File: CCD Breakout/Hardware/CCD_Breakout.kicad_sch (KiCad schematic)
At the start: 1 part

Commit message: //WIP CCD Breakout
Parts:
- added J1: Conn_01x03_Pin, symbol Connector:Conn_01x03_Pin
- added Q1: BSS138, Package_TO_SOT_SMD:SOT-23, symbol Transistor_FET:BSS138
- U1: value ~ -> ILX511
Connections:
- net +5V: now also J1.1 (Pin_1)
- net GND: now also J1.3 (Pin_3), Q1.1 (G)
- net SHSW: now also J1.2 (Pin_2)
- removed net NC: U1.10 (NC), U1.13 (NC), U1.14 (NC), U1.7 (NC), U1.8 (NC)
- no-connect marks 0 -> 5

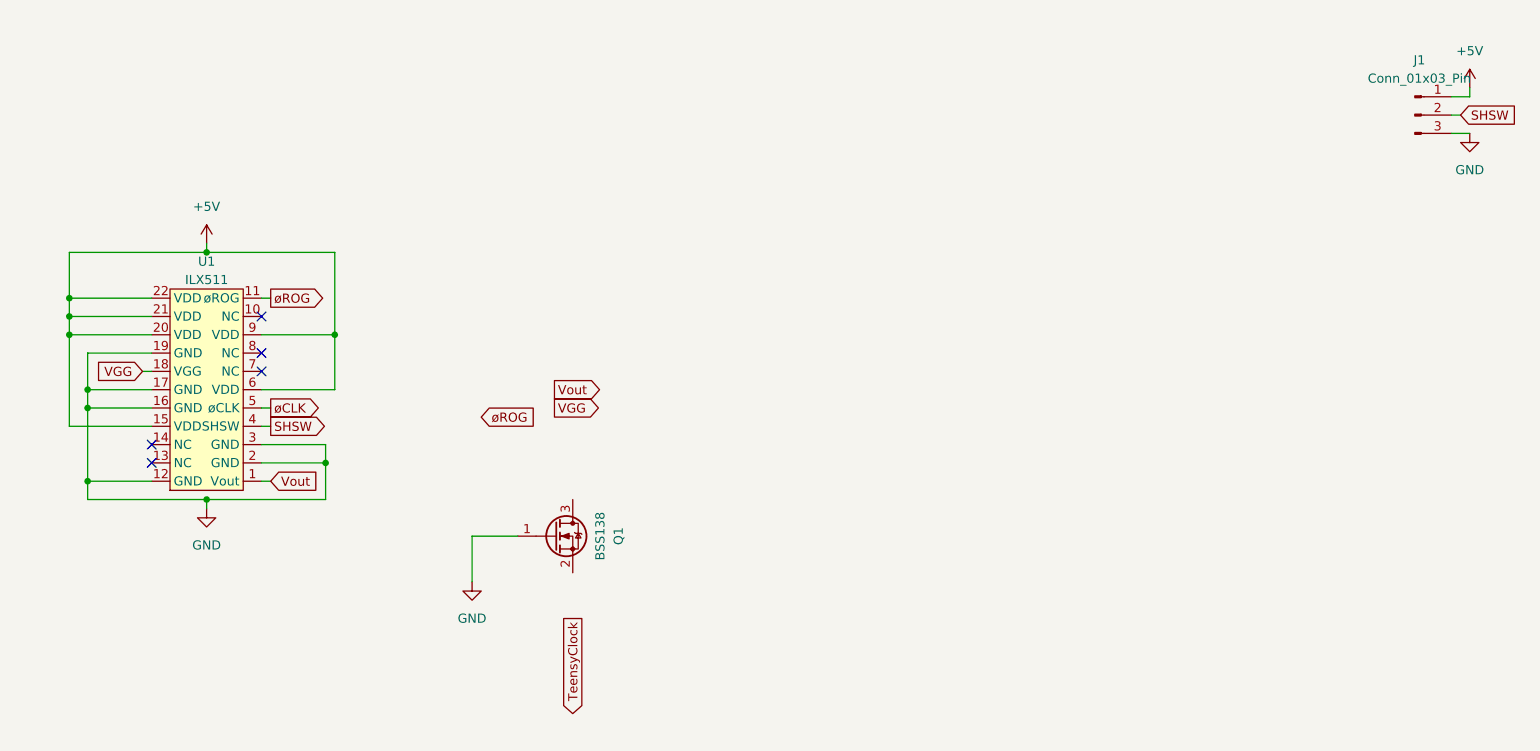
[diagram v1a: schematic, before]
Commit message: Finshed CCD breakout
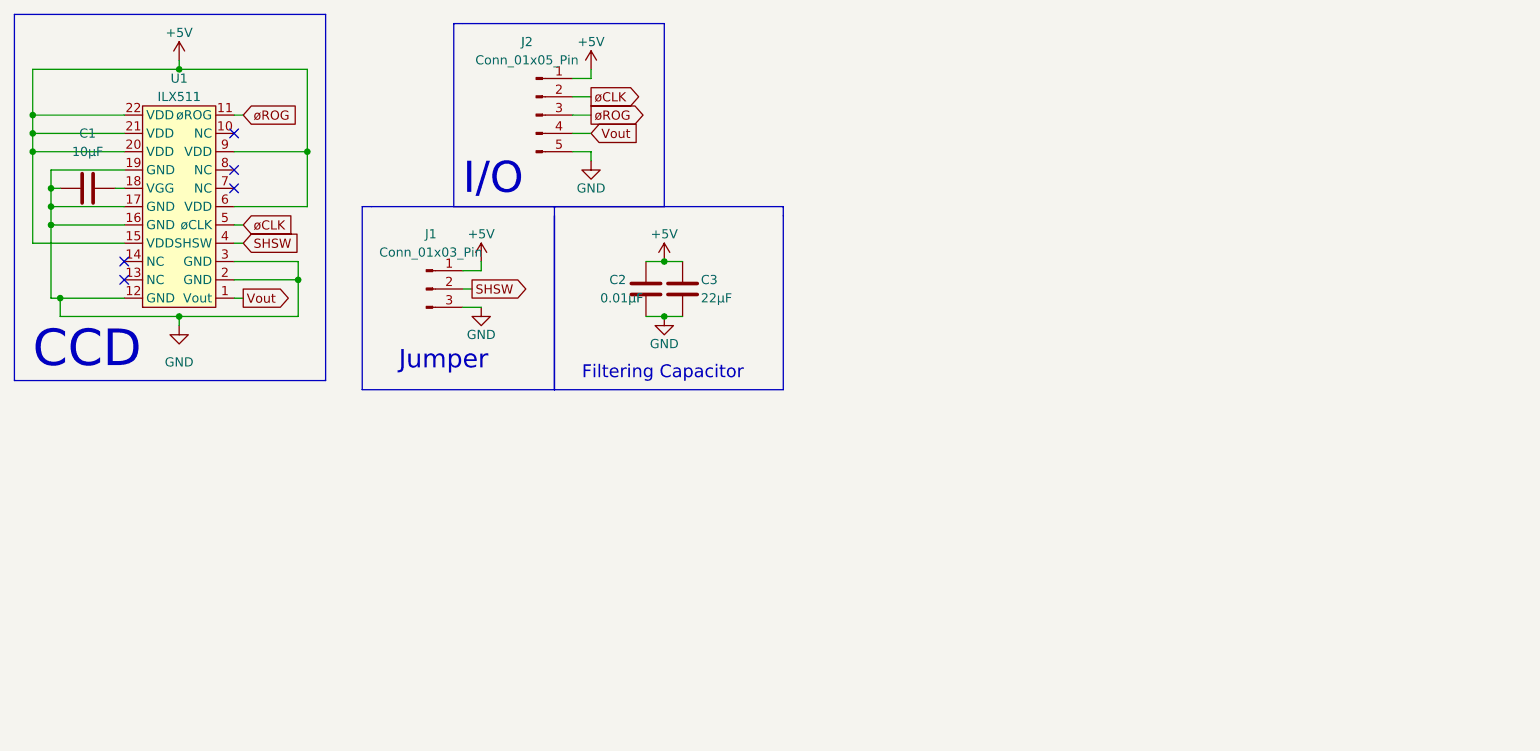
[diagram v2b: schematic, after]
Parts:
- removed Q1: BSS138, Package_TO_SOT_SMD:SOT-23, symbol Transistor_FET:BSS138
- added C1: 10µF, symbol Device:C
- added C2: 0.01µF, symbol Device:C
- added C3: 22µF, symbol Device:C
- added J2: Conn_01x05_Pin, symbol Connector:Conn_01x05_Pin
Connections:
- net +5V: now also C2.2, C3.2, J2.1 (Pin_1)
- net GND: now also C1.1, C2.1, C3.1, J2.5 (Pin_5)
- net Vout: now also J2.4 (Pin_4)
- net øCLK: now also J2.2 (Pin_2)
- net øROG: now also J2.3 (Pin_3)
- net VGG: no longer names the net of U1.18 (VGG)
- net VGG: now also C1.2
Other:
- note added: "CCD"
- note added: "Filtering Capacitor"
- note added: "I/O"
- note added: "Jumper"
- company: (none) ->  
- title: (none) -> Ramen CCD Breakout 
- moved on the sheet: J1, U1

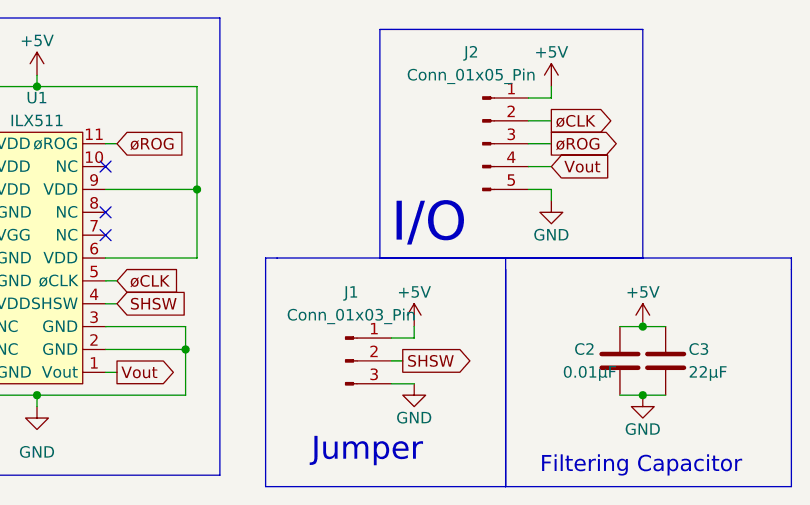
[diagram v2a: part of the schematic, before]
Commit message: fix: switched connectors to Molex
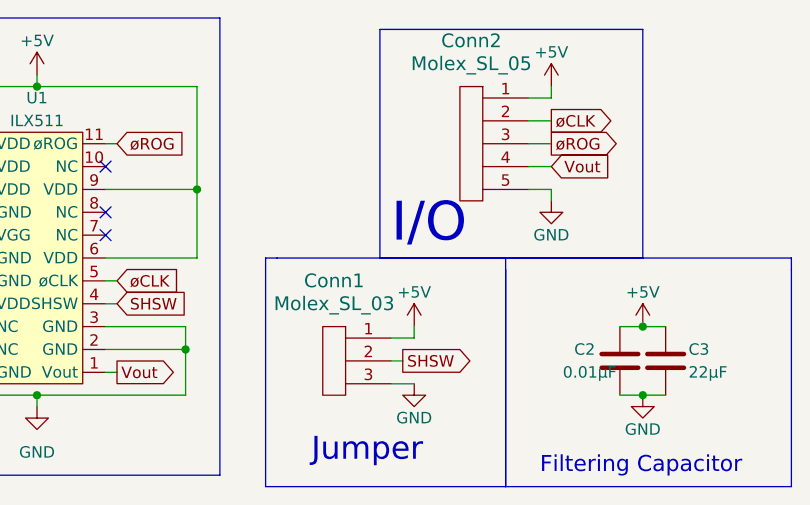
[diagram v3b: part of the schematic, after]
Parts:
- removed J1: Conn_01x03_Pin, symbol Connector:Conn_01x03_Pin
- removed J2: Conn_01x05_Pin, symbol Connector:Conn_01x05_Pin
- added Conn1: Molex_SL_03, symbol MRDT_Connectors:Molex_SL_03
- added Conn2: Molex_SL_05, symbol MRDT_Connectors:Molex_SL_05
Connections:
- net +5V: now also Conn1.1, Conn2.1
- net GND: now also Conn1.3, Conn2.5
- net SHSW: now also Conn1.2
- net Vout: now also Conn2.4
- net øCLK: now also Conn2.2
- net øROG: now also Conn2.3
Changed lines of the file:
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@@
-    )
-  )
-  (symbol (lib_id "Connector:Conn_01x05_Pin") (at 85.09 26.67 0) (unit 1)
-    (in_bom yes) (on_board yes) (dnp no)
-    (property "Reference" "J2" (at 83.82 16.51 0)
-      (effects (font (size 1.27 1.27)))
-    )
-    (property "Value" "Conn_01x05_Pin" (at 83.82 19.05 0)
-      (effects (font (size 1.27 1.27)))
-    )
-    (property "Footprint" "" (at 85.09 26.67 0)
-      (effects (font (size 1.27 1.27)) hide)
-    )
-    (property "Datasheet" "~" (at 85.09 26.67 0)
-      (effects (font (size 1.27 1.27)) hide)
-    )
-    (pin "1")
-    (pin "2")
-    (pin "3")
-    (pin "4")
-    (pin "5")
-    (instances
-      (project "CCD_Breakout"
-        (path "/64b006a0-b432-4c05-bc21-eb3325874dfb"
-          (reference "J2") (unit 1)
-        )
-      )
     )
   )
@@
     )
   )
-  (symbol (lib_id "Connector:Conn_01x03_Pin") (at 69.85 50.8 0) (unit 1)
-    (in_bom yes) (on_board yes) (dnp no)
-    (property "Reference" "J1" (at 70.485 43.18 0)
-      (effects (font (size 1.27 1.27)))
+  (symbol (lib_id "MRDT_Connectors:Molex_SL_03") (at 69.85 54.61 0) (mirror y) (unit 1)
+    (in_bom yes) (on_board yes) (dnp no) (fields_autoplaced)
+    (property "Reference" "Conn1" (at 68.58 41.91 0)
+      (effects (font (size 1.524 1.524)))
     )
-    (property "Value" "Conn_01x03_Pin" (at 70.485 45.72 0)
-      (effects (font (size 1.27 1.27)))
+    (property "Value" "Molex_SL_03" (at 68.58 44.45 0)
+      (effects (font (size 1.524 1.524)))
     )
-    (property "Footprint" "" (at 69.85 50.8 0)
-      (effects (font (size 1.27 1.27)) hide)
+    (property "Footprint" "" (at 69.85 54.61 0)
+      (effects (font (size 1.524 1.524)) hide)
     )
-    (property "Datasheet" "~" (at 69.85 50.8 0)
-      (effects (font (size 1.27 1.27)) hide)
+    (property "Datasheet" "" (at 69.85 54.61 0)
+      (effects (font (size 1.524 1.524)) hide)
     )
     (pin "1")
@@
       (project "CCD_Breakout"
         (path "/64b006a0-b432-4c05-bc21-eb3325874dfb"
-          (reference "J1") (unit 1)
+          (reference "Conn1") (unit 1)
         )
       )
@@
         )
       )
+    )
+  )
+  (symbol (lib_id "MRDT_Connectors:Molex_SL_05") (at 85.09 33.02 0) (mirror y) (unit 1)
+    (in_bom yes) (on_board yes) (dnp no) (fields_autoplaced)
+    (property "Reference" "Conn2" (at 83.82 15.24 0)
+      (effects (font (size 1.524 1.524)))
+    )
+    (property "Value" "Molex_SL_05" (at 83.82 17.78 0)
+      (effects (font (size 1.524 1.524)))
+    )
+    (property "Footprint" "" (at 85.09 33.02 0)
+      (effects (font (size 1.524 1.524)) hide)
+    )
+    (property "Datasheet" "" (at 85.09 33.02 0)
+      (effects (font (size 1.524 1.524)) hide)
+    )
+    (pin "1")
+    (pin "2")
+    (pin "3")
+    (pin "4")
+    (pin "5")
+    (instances
+      (project "CCD_Breakout"
+        (path "/64b006a0-b432-4c05-bc21-eb3325874dfb"
+          (reference "Conn2") (unit 1)
+        )
+      )

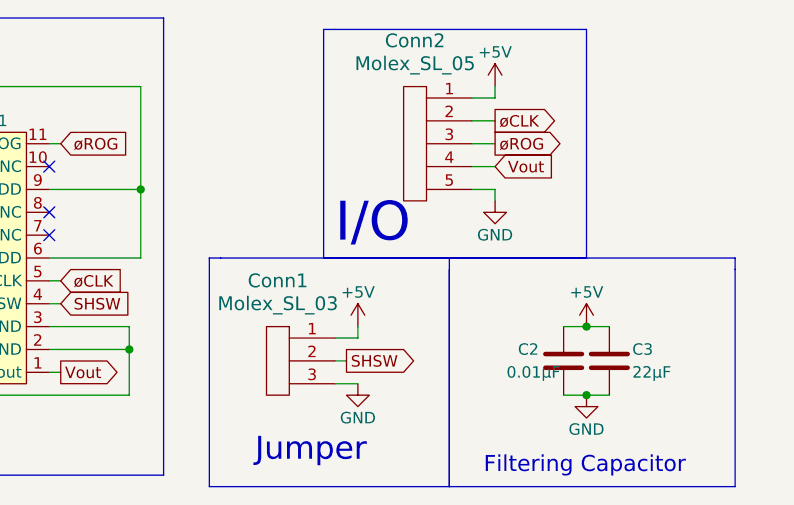
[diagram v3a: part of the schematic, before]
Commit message: fix: replaced net labels with text
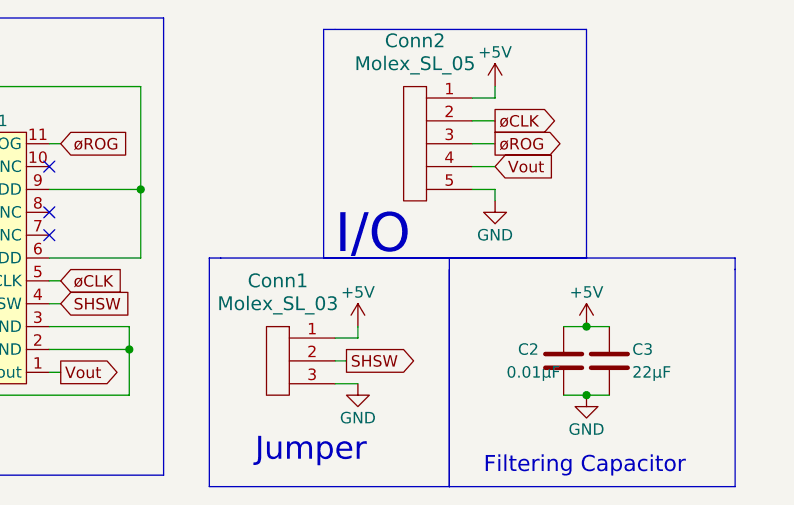
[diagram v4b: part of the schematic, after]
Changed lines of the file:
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@@
     (effects (font (size 1.778 1.778)) (justify left bottom))
   )
-  (text "I/O" (at 74.93 38.1 0)
+  (text "I/O" (at 74.93 39.37 0)
     (effects (font (size 4.318 4.318)) (justify left bottom))
   )

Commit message: misc schematic review changes
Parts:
- removed Conn1: Molex_SL_03, symbol MRDT_Connectors:Molex_SL_03
- added J1: Conn_01x03_Pin, symbol Connector:Conn_01x03_Pin
- renumbered Conn2 to Conn1
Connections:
- net +5V: now also J1.1 (Pin_1)
- net GND: now also J1.3 (Pin_3)
- net SHSW: now also J1.2 (Pin_2)
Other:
- moved on the sheet: C2, C3, Conn1

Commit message: fix: use mosfets to control diodes
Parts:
- Conn1: footprint (none) -> MRDT_Connectors:MOLEX_SL_05_Vertical
- J1: footprint (none) -> Connector_PinHeader_2.54mm:PinHeader_1x03_P2.54mm_Vertical
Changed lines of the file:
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@@
       (effects (font (size 1.27 1.27)))
     )
-    (property "Footprint" "" (at 69.85 48.26 0)
+    (property "Footprint" "Connector_PinHeader_2.54mm:PinHeader_1x03_P2.54mm_Vertical" (at 69.85 48.26 0)
       (effects (font (size 1.27 1.27)) hide)
     )
@@
       (effects (font (size 1.524 1.524)))
     )
-    (property "Footprint" "" (at 100.33 55.88 0)
+    (property "Footprint" "MRDT_Connectors:MOLEX_SL_05_Vertical" (at 100.33 55.88 0)
       (effects (font (size 1.524 1.524)) hide)
     )

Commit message: added footprints to ccd breakout
added all capacitors
the only footprint left is the ccd
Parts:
- C1, C2: footprint (none) -> Capacitor_SMD:C_0603_1608Metric_Pad1.08x0.95mm_HandSolder
- C3: footprint (none) -> Capacitor_SMD:C_0201_0603Metric_Pad0.64x0.40mm_HandSolder
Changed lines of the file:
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@@
       (effects (font (size 1.27 1.27)))
     )
-    (property "Footprint" "" (at 26.67 35.8648 0)
+    (property "Footprint" "Capacitor_SMD:C_0603_1608Metric_Pad1.08x0.95mm_HandSolder" (at 26.67 35.8648 0)
       (effects (font (size 1.27 1.27)) hide)
     )
@@
       (effects (font (size 1.27 1.27)) (justify right))
     )
-    (property "Footprint" "" (at 70.1548 24.13 0)
+    (property "Footprint" "Capacitor_SMD:C_0603_1608Metric_Pad1.08x0.95mm_HandSolder" (at 70.1548 24.13 0)
       (effects (font (size 1.27 1.27)) hide)
     )
@@
       (effects (font (size 1.27 1.27)) (justify right))
     )
-    (property "Footprint" "" (at 75.2348 24.13 0)
+    (property "Footprint" "Capacitor_SMD:C_0201_0603Metric_Pad0.64x0.40mm_HandSolder" (at 75.2348 24.13 0)
       (effects (font (size 1.27 1.27)) hide)
     )

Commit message: created ilx511 footprint
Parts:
- U1: footprint (none) -> MRDT_CCD:ILX511
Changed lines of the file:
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@@
       (effects (font (size 1.27 1.27)))
     )
-    (property "Footprint" "" (at 43.18 40.64 0)
+    (property "Footprint" "MRDT_CCD:ILX511" (at 43.18 40.64 0)
       (effects (font (size 1.27 1.27)) hide)
     )
